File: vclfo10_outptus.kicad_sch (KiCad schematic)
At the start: 33 parts, among them Q1 BC547, U3 TL072, U4 TL072

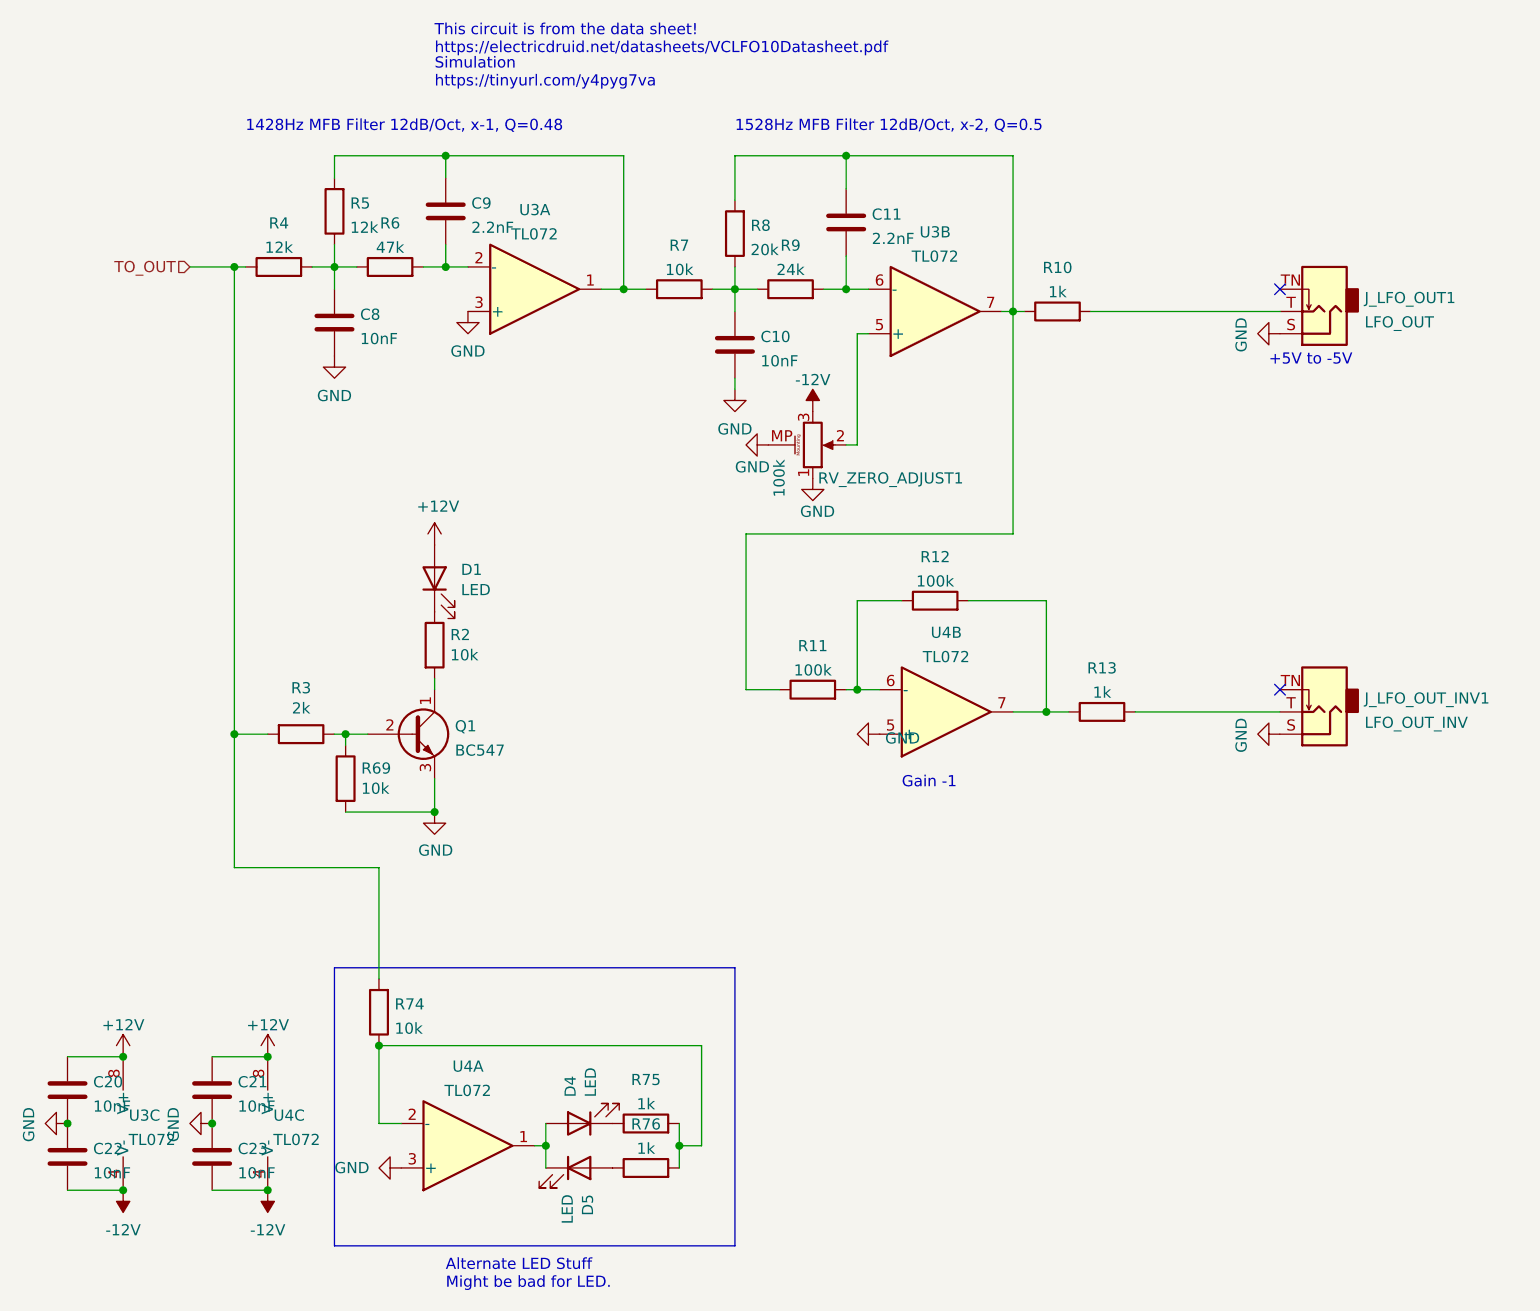
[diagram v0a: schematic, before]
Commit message: Geographic reannotate and silkscreen cleanup
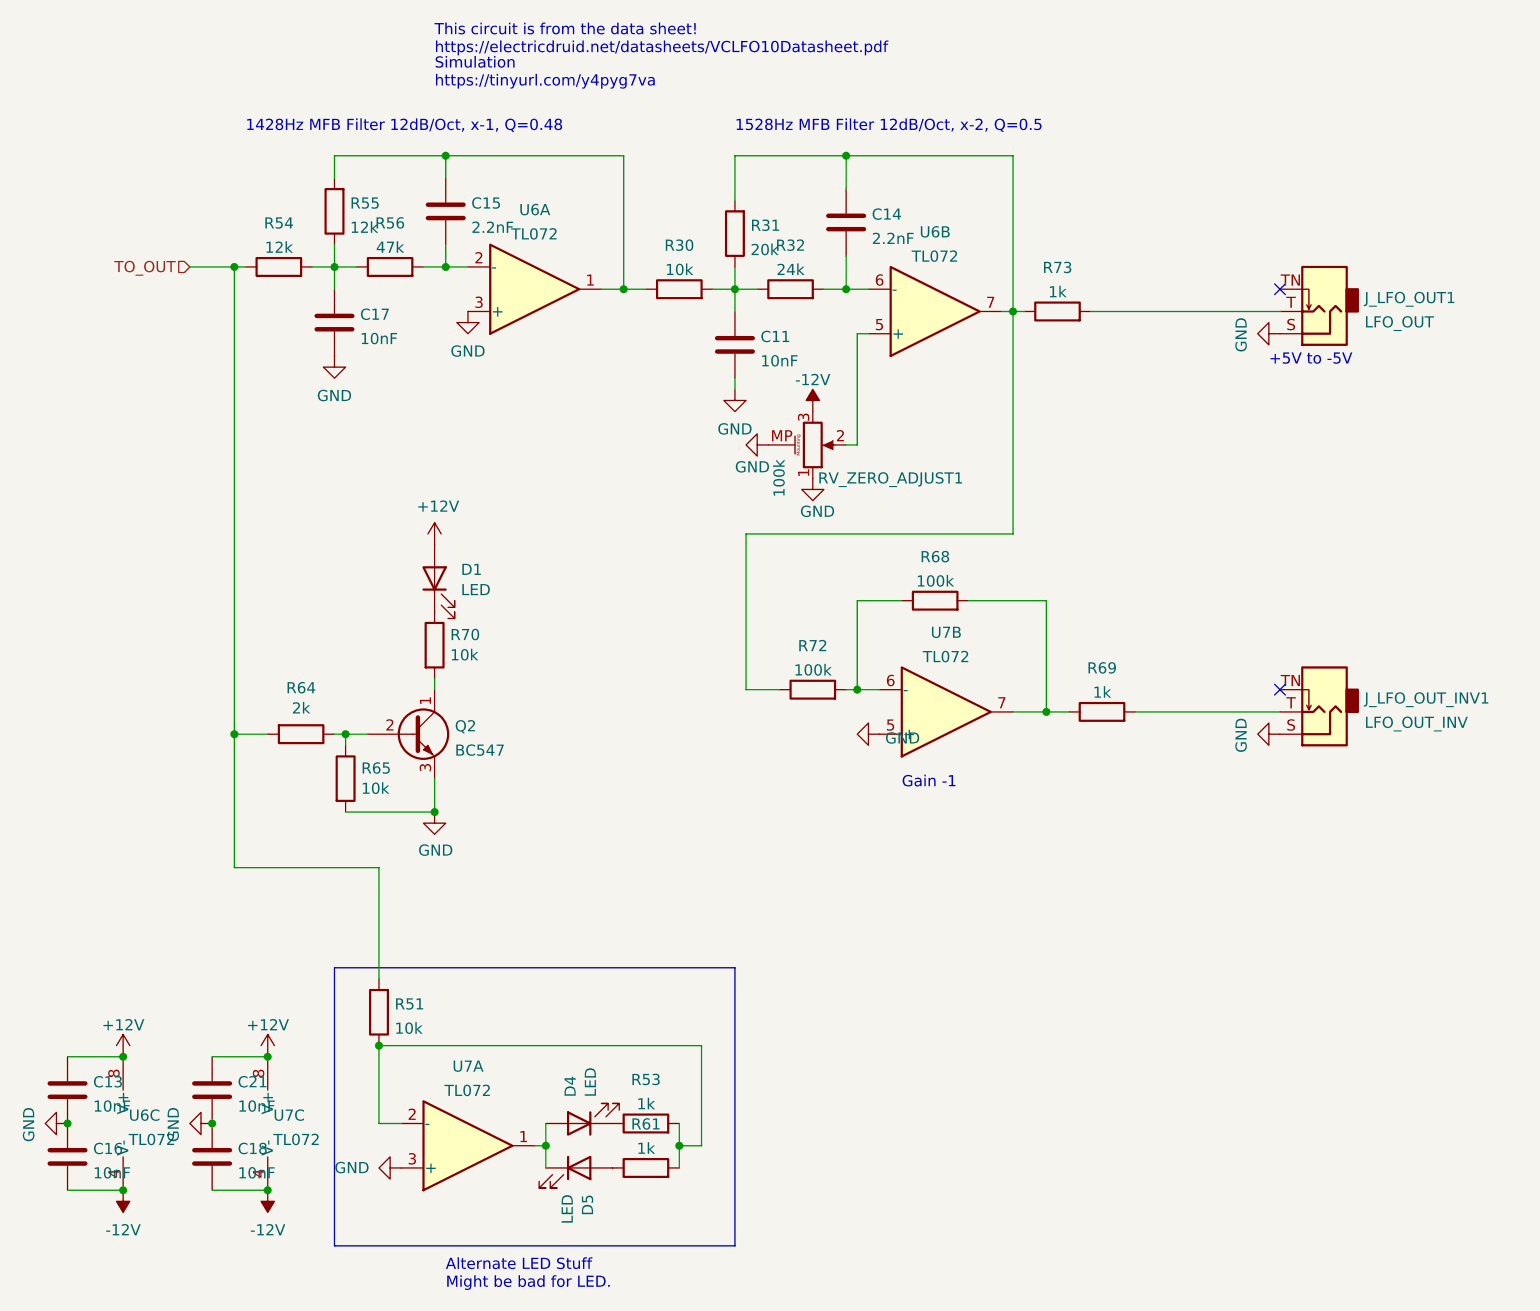
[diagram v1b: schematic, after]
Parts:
- renumbered C10 to C11, C20 to C13, C11 to C14, C9 to C15, C22 to C16, C8 to C17, C23 to C18, Q1 to Q2, R7 to R30, R8 to R31, R9 to R32, R74 to R51, R75 to R53, R4 to R54, R5 to R55, R6 to R56, R76 to R61, R3 to R64, R69 to R65, R12 to R68, R13 to R69, R2 to R70, R11 to R72, R10 to R73, U3 to U6, U4 to U7

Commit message: Update title block on schematic and pcb sheets
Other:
- title: ED VCLFO -> VCLFO10
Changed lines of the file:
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@@
   (paper "A4")
   (title_block
-    (title "ED VCLFO")
-    (date "2022-05-15")
+    (title "VCLFO10")
+    (date "2022-06-29")
     (rev "1.0")
     (company "RobotDialogs")
